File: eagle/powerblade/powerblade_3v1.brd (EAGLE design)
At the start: 25.4 x 25.4 mm, 94 parts, among them J1 JTAG_14PIN_IDC-NL, J21 AC_INSLOT2, J4 TC2030-JLINK-NL, Q1 2N7002, Q3 2SK1829, Q4 2SK1829, U1 TPS62122, U2 MCP6V3, U3 MSP430FR5738, U4 NRF51822QF, U6 MAX9910, U7 OPA2369, X1 16MHz, X3 32.768kHz, Y1 UREACH_XTEND

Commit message: well... i changed to the other type of debugging connctor. not done routing
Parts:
- removed C28: 0.1uF, rcl:C0402_SM
- removed LED2: (no value), SparkFun-LED:LED-0603
- removed R23: 120, rcl:R0402_SM
- removed TP10, TP11, TP12, TP3, TP4, TP5, TP6, TP7, TP8, TP9: TP_LONG, skyspecs:TP_LONG
- added C13: 0.1uF, passives:0402_CAP
- added SV1: (no value), con-lstb:MA12-1_1MM27
- TP1, TP2: value TP_LONG -> TP_STD; device skyspecs:TP_LONG -> skyspecs:TP
- moved TP2 40.4 mm to (-12.1, -28.3), turned to 0 degrees
- moved TP1 33.2 mm to (-12.1, -23.2)
- moved R12 0.65 mm to (10.3, -6.83)
- moved X1 0.32 mm to (-10.7, -7.62)
- moved R13 0.24 mm to (10.3, -7.70)
- moved C16 0.18 mm to (9.47, -15.7)
- moved C6 0.17 mm to (11.3, -13.5)
- moved R22 0.13 mm to (8.43, -7.59)
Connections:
- removed net N$58: LED2.A, R23.1
- removed net N$61: C39.1, R17.2, TP2.P$1, U2.P4
- removed net N$7: C10.1, C4.1, C9.1, L1.1, R24.1, R7.2, TP12.P$1, U1.P2
- new net VAMP: C39.1, R17.2, SV1.P7, U2.P4
- new net VS+: C10.1, C4.1, C9.1, L1.1, R24.1, R7.2, SV1.P12, U1.P2
- net +3V3: now also C13.1, SV1.P9, TP1.P$1; no longer C28.1, R23.2, TP11.P$1
- net FROMBLE_RX: now also SV1.P2; no longer TP7.P$1
- net GND: now also SV1.P11; no longer TP9.P$1
- net GND2: now also X1.2, X1.4
- net GND3: now also C13.2; no longer C28.2
- net I_SENSE: now also SV1.P3; no longer TP1.P$1
- net N$59: now also TP2.P$1; no longer LED2.C
- net PWM_CURRENT: now also SV1.P5; no longer TP4.P$1
- net PWM_VOLTAGE: now also SV1.P6; no longer TP5.P$1
- net TOBLE_TX: now also SV1.P1; no longer TP6.P$1
- net VCC: now also SV1.P10; no longer TP10.P$1
- net V_SENSE: now also SV1.P4; no longer TP3.P$1
- net ZC: now also SV1.P8; no longer TP8.P$1
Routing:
- net N$61: track 31.6 -> 0.00 mm, vias 1 -> 0
- net VAMP: track 0.00 -> 30.1 mm, vias 0 -> 1
- net N$7: track 23.7 -> 0.00 mm, vias 1 -> 0
- net VS+: track 0.00 -> 23.7 mm, vias 0 -> 1
- net GND: track 48.7 -> 32.9 mm
- net TOBLE_TX: track 37.4 -> 23.6 mm
- net ZC: track 26.5 -> 13.7 mm
- net N$4: track 1.51 -> 11.9 mm
- net +3V3: track 40.6 -> 30.3 mm, vias 14 -> 12
- net VCC: track 41.2 -> 31.6 mm, vias 2 -> 1
- net PWM_VOLTAGE: track 16.1 -> 8.41 mm
- net FROMBLE_RX: track 36.6 -> 29.1 mm
- net I_SENSE: track 27.1 -> 19.9 mm
- net PWM_CURRENT: track 13.6 -> 6.31 mm
- net V_SENSE: track 25.4 -> 18.4 mm
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- added copper zone on layer 1, net VS+
- removed copper zone on layer 1, net N$7

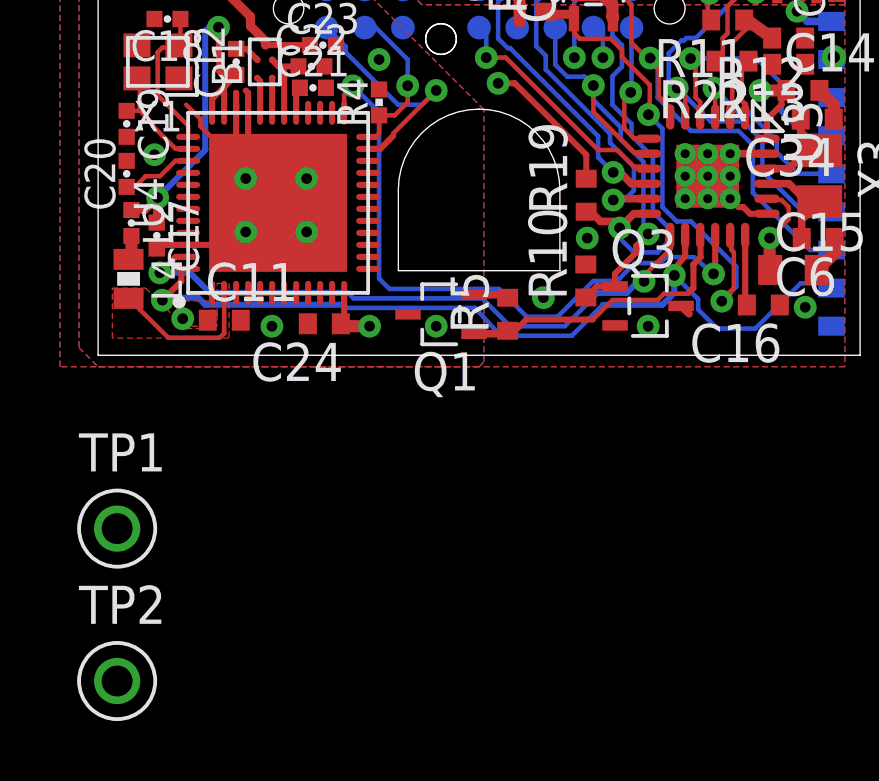
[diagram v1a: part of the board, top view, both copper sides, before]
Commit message: removed led once and for all
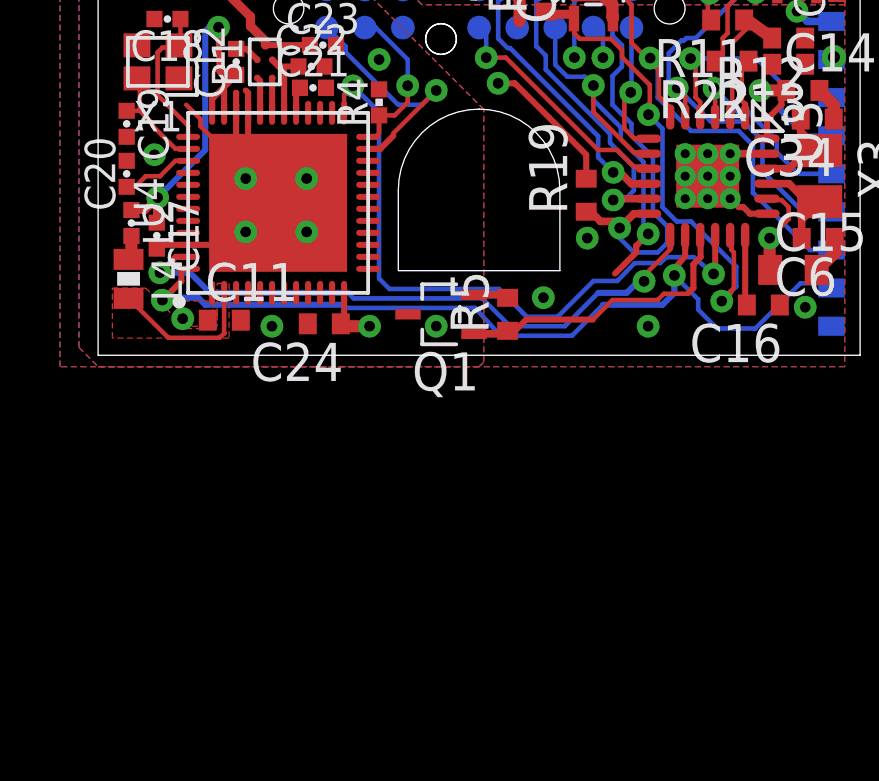
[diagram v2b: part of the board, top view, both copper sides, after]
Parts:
- removed Q3: 2SK1829, powerfilm:SC-70-3
- removed R10: 220k, rcl:R0402_SM
- removed TP1, TP2: TP_STD, skyspecs:TP
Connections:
- removed net N$59: Q3.P3, TP2.P$1
- net +3V3: no longer TP1.P$1
- net GND: no longer Q3.P2, R10.2
- net TDI: no longer Q3.P1, R10.1
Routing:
- net TDI: track 15.4 -> 13.8 mm
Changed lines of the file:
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@@
 <attribute name="DIGIKEY" value="1276-1817-1-ND" x="26.51125" y="72.771" size="1.778" layer="27" rot="R180" display="off"/>
-</element>
-<element name="Q3" library="powerfilm" package="SC-70-3" value="2SK1829" x="5.63245" y="-15.75435">
-<attribute name="DIGIKEY" value="2SK1829TE85LFCT-ND" x="-25.60955" y="-103.38435" size="1.778" layer="27" display="off"/>
 </element>
 <element name="C12" library="passives" package="0402_CAP" value="1nF" x="-8.09625" y="-7.62" rot="R90">
@@
 </element>
 <element name="R6" library="rcl" package="R0402_SM" value="660k" x="2.2225" y="-5.3975" rot="R90"/>
-<element name="R10" library="rcl" package="R0402_SM" value="220k" x="3.556" y="-14.9225" rot="R90"/>
 <element name="R13" library="rcl" package="R0402_SM" value="330k" x="10.31875" y="-7.699375" rot="R180"/>
 <element name="R22" library="rcl" package="R0402_SM" value="670k" x="8.4328" y="-7.5946" rot="R180"/>
@@
 <attribute name="DIGIKEY" value="445-1265-1-ND" x="11.90625" y="-3.96875" size="1.778" layer="27" rot="R90" display="off"/>
 </element>
-<element name="TP1" library="skyspecs" package="TP" value="TP_STD" x="-12.065" y="-23.1775"/>
-<element name="TP2" library="skyspecs" package="TP" value="TP_STD" x="-12.065" y="-28.2575"/>
 </elements>
 <signals>
@@
 <wire x1="10.63625" y1="-5.8928" x2="10.59815" y2="-5.9309" width="0.254" layer="16"/>
 <contactref element="SV1" pad="P9"/>
-<contactref element="TP1" pad="P$1"/>
 <wire x1="11.7475" y1="-6.270625" x2="10.937875" y2="-6.270625" width="0.254" layer="16"/>
 <wire x1="10.937875" y1="-6.270625" x2="10.59815" y2="-5.9309" width="0.254" layer="16"/>
-<wire x1="-9.8806" y1="-16.1798" x2="-12.065" y2="-23.1775" width="0" layer="19" extent="1-1"/>
-<wire x1="11.7475" y1="-0.67555" x2="11.86443125" y2="-5.3125" width="0" layer="19" extent="1-1"/>
+<wire x1="11.86443125" y1="-5.3125" x2="11.7475" y2="-0.67555" width="0" layer="19" extent="1-1"/>
 </signal>
 <signal name="N$37">
@@
 <contactref element="U3" pad="P8"/>
 <contactref element="J1" pad="P3"/>
-<contactref element="Q3" pad="P1"/>
-<contactref element="R10" pad="1"/>
 <wire x1="2.54" y1="-6.477" x2="2.54" y2="-7.71525" width="0.1524" layer="16"/>
 <wire x1="2.54" y1="-7.71525" x2="2.936875" y2="-8.112125" width="0.1524" layer="16"/>
 <via x="5.635625" y="-13.35405" extent="1-16" drill="0.3556"/>
-<wire x1="4.53245" y1="-15.10435" x2="3.92415" y2="-15.10435" width="0.2032" layer="1"/>
-<wire x1="3.92415" y1="-15.10435" x2="3.556" y2="-15.4725" width="0.2032" layer="1"/>
-<wire x1="4.524375" y1="-15.096275" x2="4.53245" y2="-15.10435" width="0.2032" layer="1"/>
-<wire x1="4.53245" y1="-15.10435" x2="4.53245" y2="-14.6763" width="0.2032" layer="1"/>
 <wire x1="4.53245" y1="-14.6763" x2="5.23875" y2="-13.97" width="0.2032" layer="1"/>
 <wire x1="5.23875" y1="-13.97" x2="5.23875" y2="-13.750925" width="0.2032" layer="1"/>
@@
 <wire x1="10.753" y1="-13.50645" x2="10.753" y2="-12.8808" width="0.254" layer="1"/>
 <wire x1="10.753" y1="-12.8808" x2="11.3538" y2="-12.28" width="0.254" layer="1"/>
-</signal>
-<signal name="N$59">
-<contactref element="Q3" pad="P3"/>
-<wire x1="6.73245" y1="-15.75435" x2="6.997" y2="-16.0189" width="0.254" layer="1"/>
-<contactref element="TP2" pad="P$1"/>
-<wire x1="6.73245" y1="-15.75435" x2="-12.065" y2="-28.2575" width="0" layer="19" extent="1-1"/>
 </signal>
 <signal name="N$5">
@@
 <contactref element="C6" pad="1"/>
 <contactref element="C34" pad="1"/>
-<contactref element="Q3" pad="P2"/>
 <contactref element="R5" pad="2"/>
 <contactref element="Q1" pad="P2"/>
 <contactref element="R6" pad="2"/>
 <contactref element="Q4" pad="P2"/>
-<contactref element="R10" pad="2"/>
 <contactref element="R13" pad="1"/>
 <contactref element="D1" pad="A"/>

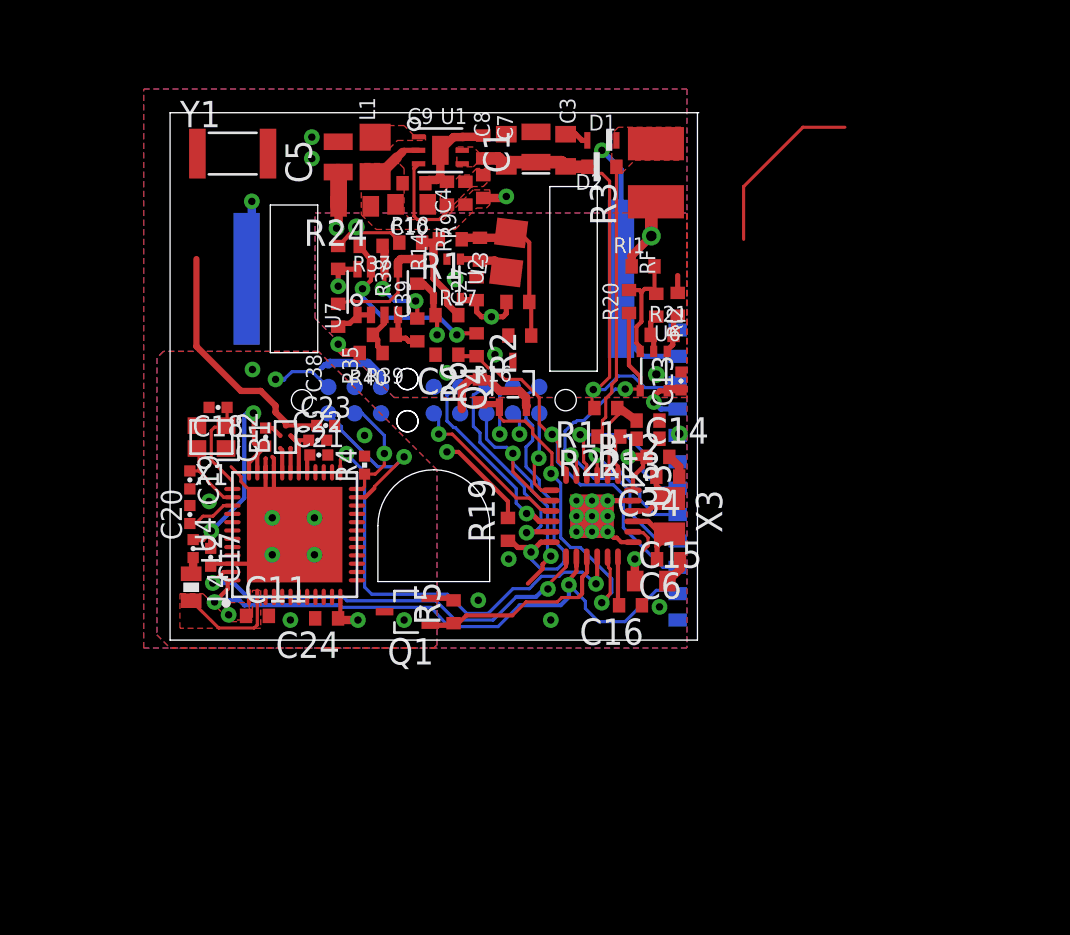
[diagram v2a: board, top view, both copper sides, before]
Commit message: finished routing supply in backwards
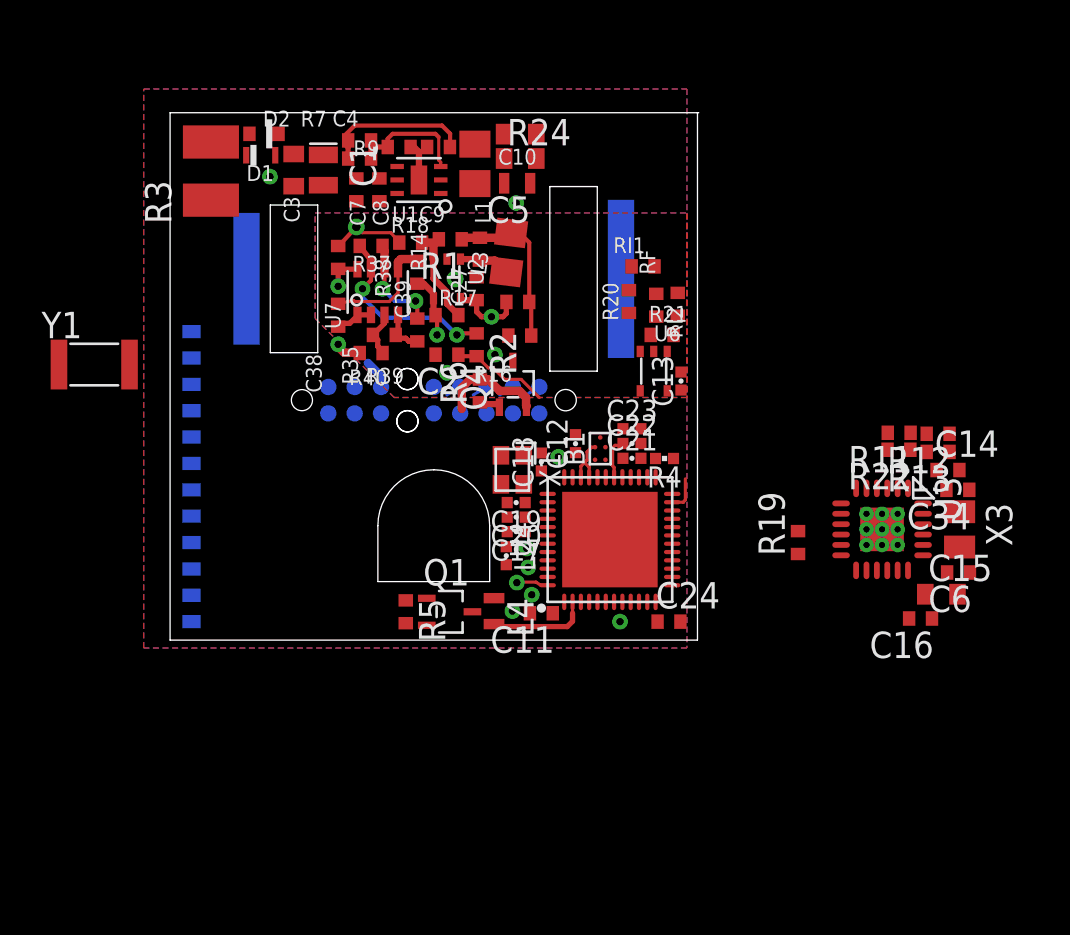
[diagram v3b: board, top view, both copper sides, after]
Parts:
- C5: device rcl:C0805_SM -> rcl:C0603_TN
- C7: device rcl:C0603_SM -> rcl:C0402_SM
- L4: device passives:0603_CAP -> rcl:C0603_TN
- moved SV1 23.4 mm to (-11.7, -9.53)
- moved R3 21.4 mm to (-10.7, 5.19)
- moved C24 16.5 mm to (11.3, -16.5), turned to 0 degrees
- moved D1 16.4 mm to (-8.33, 5.95), turned to 180 degrees
- moved D2 16.3 mm to (-8.18, 6.99), turned to 0 degrees
- moved C18 15.8 mm to (5.18, -8.82), turned to 90 degrees
- moved C19 15.8 mm to (3.97, -10.8), turned to 180 degrees
- moved C20 15.7 mm to (3.97, -11.5), turned to 180 degrees
- moved U4 15.2 mm to (8.48, -12.6)
- moved B1 15.2 mm to (8.02, -8.18)
- moved C22 15.1 mm to (9.54, -7.93)
- moved L2 15.1 mm to (3.49, -13.3)
- moved C21 15.1 mm to (9.54, -8.64)
- moved C12 14.9 mm to (6.83, -7.94)
- moved C17 14.8 mm to (3.97, -12.2), turned to 180 degrees
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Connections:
- net BLE_LPINT: now also U4.9; no longer U4.25
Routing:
- net VCC: track 31.6 -> 0.00 mm, vias 1 -> 0
- net VTEST: track 30.9 -> 0.00 mm, vias 2 -> 0
- net FROMBLE_RX: track 29.1 -> 1.54 mm, vias 2 -> 1
- net GND: track 32.9 -> 7.72 mm, vias 9 -> 1
- net TOBLE_TX: track 23.6 -> 0.00 mm, vias 2 -> 1
- net +3V3: track 30.3 -> 6.90 mm, vias 12 -> 4
- net BLE_LPINT: track 21.8 -> 0.00 mm, vias 2 -> 1
- net GND2: track 24.0 -> 4.05 mm, vias 9 -> 1
- net V_SENSE: track 18.4 -> 0.00 mm, vias 2 -> 0
- net VS+: track 23.7 -> 7.27 mm, vias 1 -> 0
- net METER_ENABLE: track 16.6 -> 1.48 mm, vias 2 -> 0
- net I_SENSE: track 19.9 -> 4.90 mm, vias 1 -> 0
- net VAMP: track 30.1 -> 15.7 mm
- net RST: track 14.6 -> 0.74 mm, vias 1 -> 0
- net TDI: track 13.8 -> 0.00 mm, vias 2 -> 0
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- removed copper zone on layer 1, net +3V3
- removed copper zone on layer 1, net DCC
- removed copper zone on layer 1, net GND2
- removed copper zone on layer 16, net GND2
- removed copper zone on layer 2, net GND2
- removed copper zone on layer 1, net N$13
- removed copper zone on layer 1, net N$9
- removed copper zone on layer 1, net VCC
- removed copper zone on layer 1, net VS+
- removed copper zone on layer 1, net ZC

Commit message: down to 9 airwires
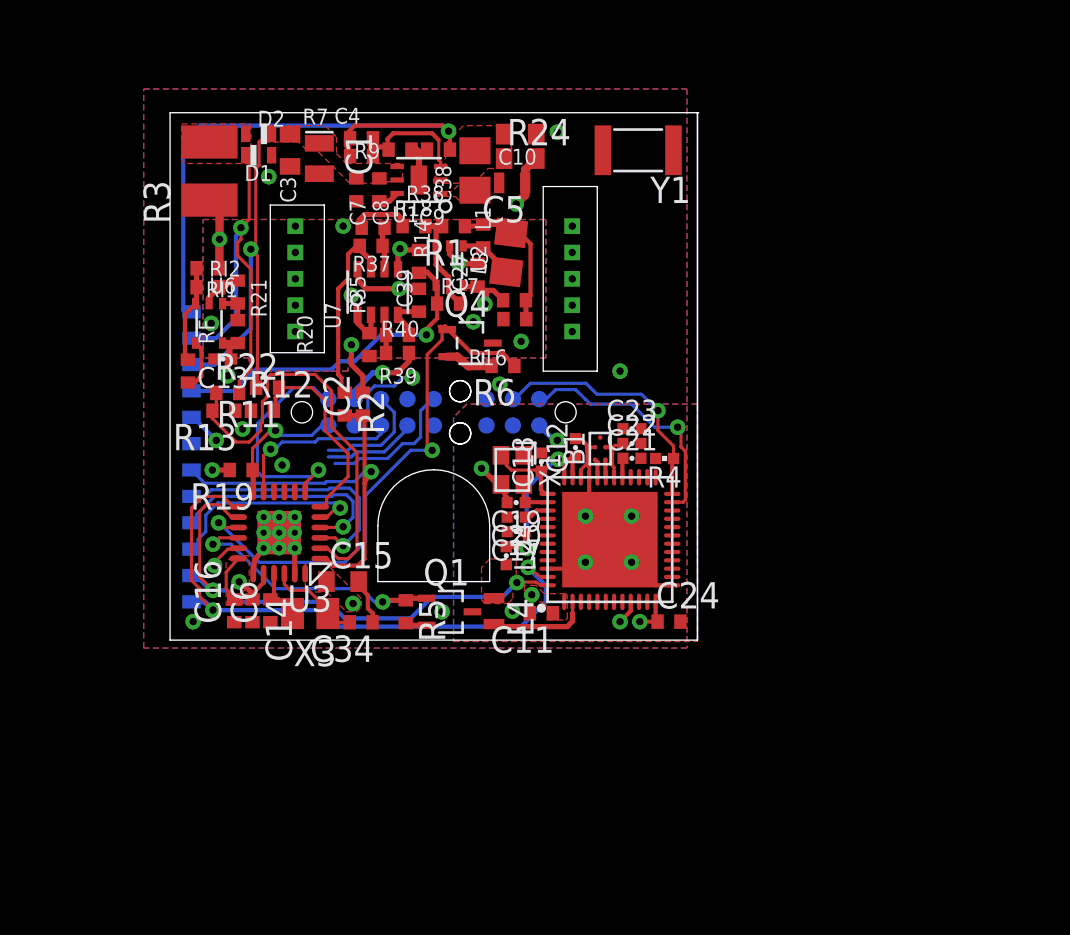
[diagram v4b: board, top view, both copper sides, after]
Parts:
- removed J21: AC_INSLOT2, powerfilm:AC3_SLOT_OUT2
- added J2: AC_INF2, powerfilm:AC3_F2
- moved R13 34.5 mm to (-10.1, -6.35)
- moved C14 34.2 mm to (-8.73, -16.0), turned to 270 degrees
- moved C6 33.2 mm to (-7.87, -16.0), turned to 90 degrees
- moved C16 33.1 mm to (-9.61, -16.0), turned to 90 degrees
- moved R12 32.6 mm to (-8.26, -6.35), turned to 0 degrees
- moved R22 32.4 mm to (-9.92, -5.49), turned to 0 degrees
- moved X3 31.5 mm to (-5.95, -16.1), turned to 180 degrees
- moved R11 30.5 mm to (-8.00, -5.24)
- moved C34 29.4 mm to (-3.50, -16.5)
- moved U3 29.0 mm to (-7.45, -12.2), turned to 180 degrees
- moved C15 28.8 mm to (-4.39, -14.6)
- moved Y1 28.2 mm to (9.84, 6.19), turned to 180 degrees
- moved R19 27.0 mm to (-9.28, -9.21), turned to 180 degrees
- moved C13 22.1 mm to (-10.2, -3.86), turned to 180 degrees
- moved RI2 21.6 mm to (-10.9, -0.40), turned to 180 degrees
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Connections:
- net TDO renamed N$2
- net +3V3: now also SV1.P8; no longer SV1.P9
- net BLE_ENABLE: now also U3.P16; no longer U3.P15
- net BLE_LPINT: now also U3.P17; no longer U3.P16
- net GND: now also J2.P2A, J2.P2B, J2.P2C, J2.P2D, J2.P2E, SV1.P7; no longer J21.N, SV1.P11
- net I_SENSE: now also SV1.P6, U3.P1; no longer SV1.P3, U3.P6
- net METER_ENABLE: now also U3.P15; no longer U3.P17
- net PWM_VOLTAGE: now also SV1.P4; no longer SV1.P6
- net VAMP: now also SV1.P9; no longer SV1.P7
- net VCC_SENSE: now also U3.P6; no longer U3.P2
- net VTEST: now also J2.P1A, J2.P1B, J2.P1C, J2.P1D, J2.P1E; no longer J21.P
- net V_SENSE: now also SV1.P3; no longer SV1.P4
- net ZC: now also SV1.P11; no longer SV1.P8
- net ZC_LOW: now also U3.P2; no longer U3.P1
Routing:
- net TOBLE_TX: track 0.00 -> 29.4 mm, vias 1 -> 2
- net METER_ENABLE: track 1.48 -> 26.8 mm, vias 0 -> 2
- net BLE_LPINT: track 0.00 -> 24.4 mm, vias 1 -> 2
- net FROMBLE_RX: track 1.54 -> 25.1 mm, vias 1 -> 2
- net VS+: track 7.27 -> 29.5 mm, vias 0 -> 1
- net ZC_LOW: track 0.00 -> 20.8 mm
- net VCC: track 0.00 -> 20.5 mm, vias 0 -> 1
- net ZC: track 0.00 -> 19.2 mm, vias 0 -> 1
- net VTEST: track 0.00 -> 18.5 mm, vias 0 -> 1
- net +3V3: track 6.90 -> 23.6 mm, vias 4 -> 12
- net I_SENSE: track 4.90 -> 20.0 mm, vias 0 -> 1
- net BLE_ENABLE: track 0.00 -> 12.9 mm, vias 0 -> 2
- net V_SENSE: track 0.00 -> 12.7 mm, vias 0 -> 1
- net PWM_CURRENT: track 0.00 -> 12.3 mm, vias 0 -> 1
- net SWDCLK: track 0.00 -> 12.2 mm, vias 0 -> 1
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- added copper zone on layer 1, net +3V3
- added copper zone on layer 1, net GND2
- added copper zone on layer 16, net GND2
- added copper zone on layer 2, net GND2
- added copper zone on layer 1, net N$10
- added copper zone on layer 1, net N$23
- added copper zone on layer 1, net N$9
- added copper zone on layer 1, net VCC
- added copper zone on layer 1, net VS+
- added copper zone on layer 1, net ZC
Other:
- outline, holes or cut-outs redrawn
